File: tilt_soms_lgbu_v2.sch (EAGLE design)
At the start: 37 parts

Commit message: Added a v2 for the tilt_soms_lgbu board (tilt_soms_lgbu_v2)
Primary changes:
Placed all components on top layer including the con-wago connectors.
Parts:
- SOMS: value (none) -> JST-PH_3-PIN_HEADER; device con-wago-500:W237-103 -> SRG:JST-PH_3-PIN_HEADER
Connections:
- net FEATHER_3.3V: now also SOMS.3; no longer SOMS-1.KL
- net GND: now also SOMS.1; no longer SOMS-3.KL
- net GPIOA3: now also SOMS.2; no longer SOMS-2.KL
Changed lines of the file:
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@@
 <part name="C4" library="rcl" deviceset="C-US" device="C1812"/>
 <part name="MAIN_SWITCH" library="SRG" deviceset="JST-PH_2-PIN_HEADER" device=""/>
-<part name="SOMS" library="con-wago-500" deviceset="W237-103" device=""/>
 <part name="H5" library="holes" library_urn="urn:adsk.eagle:library:237" deviceset="MOUNT-HOLE" device="2.8" package3d_urn="urn:adsk.eagle:package:14271/1"/>
 <part name="H6" library="holes" library_urn="urn:adsk.eagle:library:237" deviceset="MOUNT-HOLE" device="2.8" package3d_urn="urn:adsk.eagle:package:14271/1"/>
 <part name="H7" library="holes" library_urn="urn:adsk.eagle:library:237" deviceset="MOUNT-HOLE" device="2.8" package3d_urn="urn:adsk.eagle:package:14271/1"/>
 <part name="H8" library="holes" library_urn="urn:adsk.eagle:library:237" deviceset="MOUNT-HOLE" device="2.8" package3d_urn="urn:adsk.eagle:package:14271/1"/>
+<part name="SOMS" library="SRG" deviceset="JST-PH_3-PIN_HEADER" device=""/>
 </parts>
 <sheets>
@@
 <instance part="C4" gate="G$1" x="320.04" y="215.9"/>
 <instance part="MAIN_SWITCH" gate="G$1" x="160.02" y="101.6" smashed="yes" rot="R90"/>
-<instance part="SOMS" gate="-1" x="287.02" y="132.08"/>
-<instance part="SOMS" gate="-2" x="287.02" y="127"/>
-<instance part="SOMS" gate="-3" x="287.02" y="121.92"/>
 <instance part="H5" gate="G$1" x="20.32" y="63.5"/>
 <instance part="H6" gate="G$1" x="20.32" y="55.88"/>
 <instance part="H7" gate="G$1" x="20.32" y="71.12"/>
 <instance part="H8" gate="G$1" x="20.32" y="78.74"/>
+<instance part="SOMS" gate="G$1" x="271.78" y="127" rot="R180"/>
 </instances>
 <busses>
@@
 </segment>
 <segment>
-<wire x1="299.72" y1="124.46" x2="309.88" y2="124.46" width="0.1524" layer="91"/>
-<pinref part="SOMS" gate="-3" pin="KL"/>
-<wire x1="299.72" y1="124.46" x2="299.72" y2="121.92" width="0.1524" layer="91"/>
-<wire x1="299.72" y1="121.92" x2="292.1" y2="121.92" width="0.1524" layer="91"/>
+<pinref part="SOMS" gate="G$1" pin="1"/>
+<wire x1="276.86" y1="124.46" x2="309.88" y2="124.46" width="0.1524" layer="91"/>
 </segment>
 <segment>
@@
 </segment>
 <segment>
-<wire x1="294.64" y1="129.54" x2="309.88" y2="129.54" width="0.1524" layer="91"/>
 <label x="299.72" y="129.54" size="1.778" layer="95"/>
-<wire x1="294.64" y1="129.54" x2="294.64" y2="132.08" width="0.1524" layer="91"/>
-<pinref part="SOMS" gate="-1" pin="KL"/>
-<wire x1="294.64" y1="132.08" x2="292.1" y2="132.08" width="0.1524" layer="91"/>
+<pinref part="SOMS" gate="G$1" pin="3"/>
+<wire x1="276.86" y1="129.54" x2="309.88" y2="129.54" width="0.1524" layer="91"/>
 </segment>
 </net>
@@
 </segment>
 <segment>
-<wire x1="292.1" y1="127" x2="320.04" y2="127" width="0.1524" layer="91"/>
+<wire x1="276.86" y1="127" x2="320.04" y2="127" width="0.1524" layer="91"/>
 <label x="322.58" y="127" size="1.778" layer="95" rot="R180"/>
-<pinref part="SOMS" gate="-2" pin="KL"/>
-</segment>
-</net>
+<pinref part="SOMS" gate="G$1" pin="2"/>
+</segment>
+</net>

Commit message: Reversed board. Snap to mills grid.
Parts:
- removed H5, H6, H7, H8: MOUNT-HOLE2.8, holes:MOUNT-HOLE2.8
- R1, R2, R3, R4: device rcl:R-EU_0204/5 -> rcl:R-EU_0204/7
- SOMS: value JST-PH_3-PIN_HEADER -> TERMINAL-BLOCK-3.5MM-3-PIN-LONG-PAD; device SRG:JST-PH_3-PIN_HEADER -> Rembrandt Electronics - Terminal Block 3-5mm v1-0:TERMINAL-BLOCK-3.5MM-3-PIN-LONG-PAD
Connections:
- net FEATHER_3.3V: now also SOMS-3.K; no longer SOMS.3
- net GND: now also SOMS-1.K; no longer SOMS.1
- net GPIOA3: now also SOMS-2.K; no longer SOMS.2
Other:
- moved on the sheet: U$3

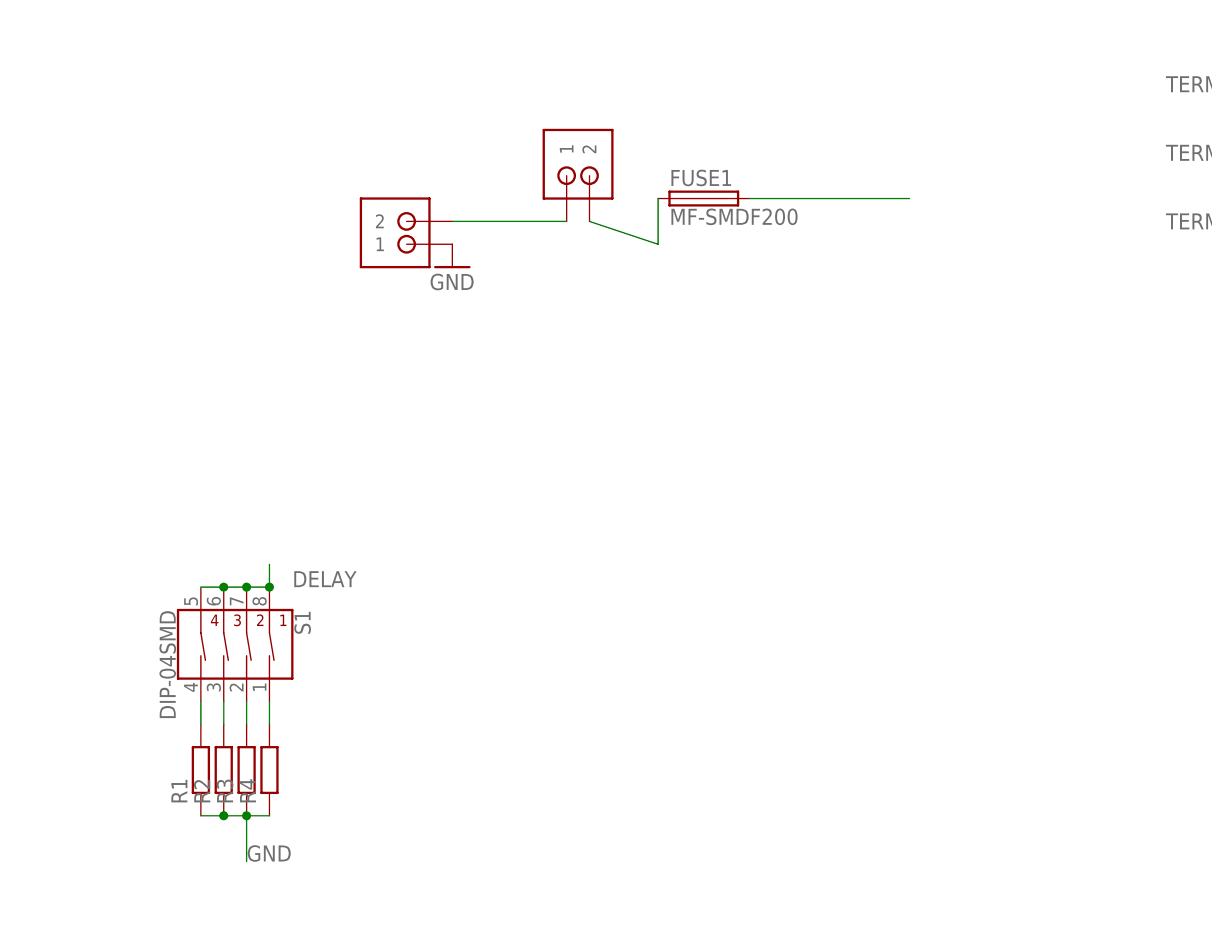
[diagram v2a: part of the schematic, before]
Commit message: no dip switch
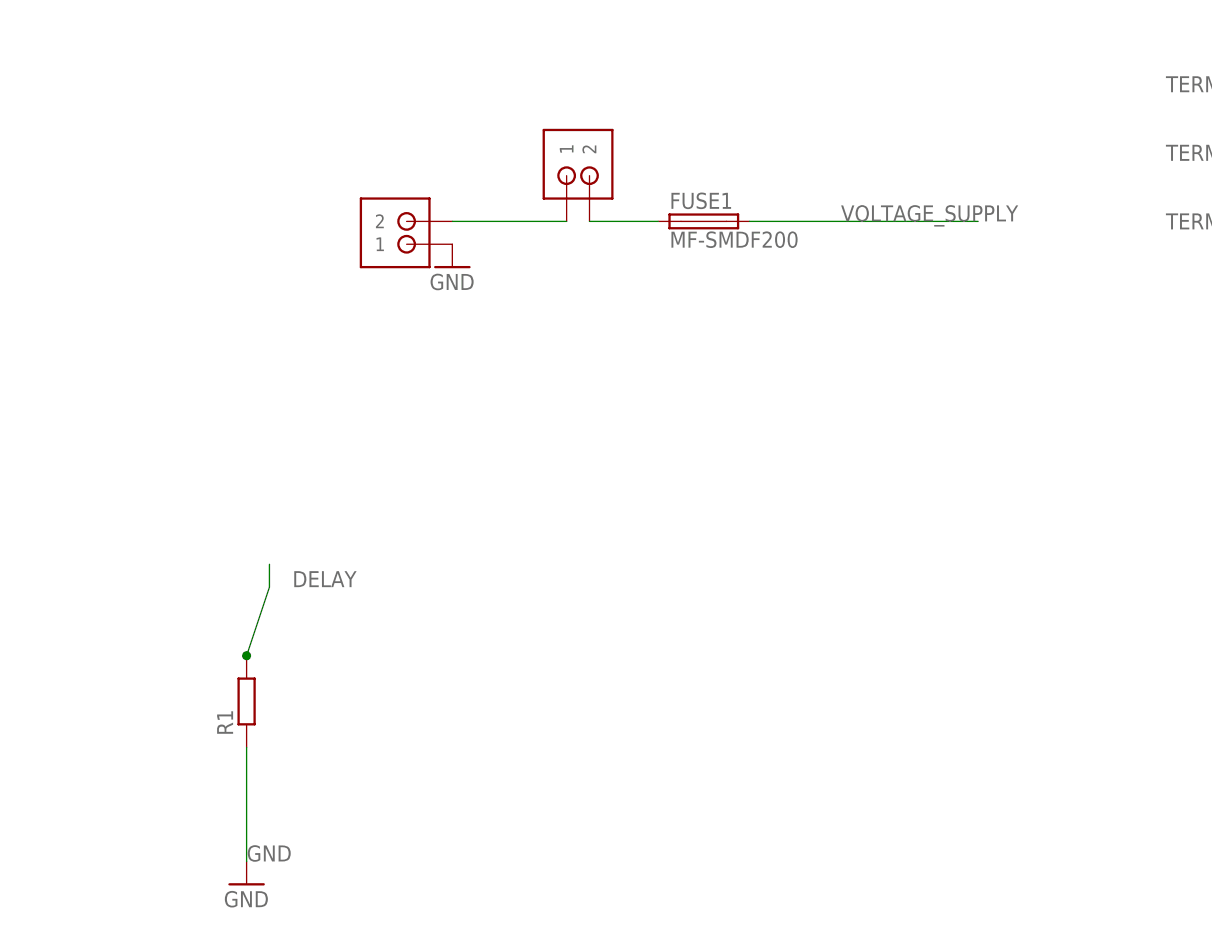
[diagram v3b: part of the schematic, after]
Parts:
- removed R2, R3, R4: (no value), rcl:R-EU_0204/7
- removed S1: DIP-04SMD, SparkFun-Switches:DIP-04SMD
- R1: device rcl:R-EU_0204/7 -> rcl:R-EU_0309/12
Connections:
- removed net N$10: R2.2, S1.3A
- removed net N$11: R3.2, S1.2A
- removed net N$12: R4.2, S1.1A
- removed net N$9: R1.2, S1.4A
- net DELAY: now also R1.2; no longer S1.1B, S1.2B, S1.3B, S1.4B
- net GND: no longer R2.1, R3.1, R4.1
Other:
- moved on the sheet: FUSE1, R1
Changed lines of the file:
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@@
 <part name="BATT" library="SRG" deviceset="JST-PH_2-PIN_HEADER" device=""/>
 <part name="U$3" library="edc_modules" deviceset="TPL5110_BREAKOUT" device=""/>
-<part name="S1" library="SparkFun-Switches" deviceset="DIP-04" device="SMD"/>
-<part name="R1" library="rcl" deviceset="R-EU_" device="0204/7"/>
-<part name="R2" library="rcl" deviceset="R-EU_" device="0204/7"/>
-<part name="R3" library="rcl" deviceset="R-EU_" device="0204/7"/>
-<part name="R4" library="rcl" deviceset="R-EU_" device="0204/7"/>
+<part name="R1" library="rcl" deviceset="R-EU_" device="0309/12"/>
 <part name="FRAME2" library="frames" deviceset="DINA4_L" device=""/>
 <part name="U$4" library="edc_modules" deviceset="BNO05_BREAKOUT" device=""/>
@@
 <part name="MAIN_SWITCH" library="SRG" deviceset="JST-PH_2-PIN_HEADER" device=""/>
 <part name="SOMS" library="Rembrandt Electronics - Terminal Block 3-5mm v1-0" deviceset="TERMINAL-BLOCK-3.5MM-3-PIN" device="-LONG-PAD"/>
+<part name="GND1" library="supply1" deviceset="GND" device=""/>
 </parts>
 <sheets>
@@
 <instance part="BATT" gate="G$1" x="137.16" y="93.98" smashed="yes" rot="R180"/>
 <instance part="U$3" gate="G$1" x="96.52" y="137.16"/>
-<instance part="S1" gate="G$1" x="127" y="50.8" rot="R180"/>
-<instance part="R1" gate="G$1" x="116.84" y="33.02" rot="R90"/>
-<instance part="R2" gate="G$1" x="119.38" y="33.02" rot="R90"/>
-<instance part="R3" gate="G$1" x="121.92" y="33.02" rot="R90"/>
-<instance part="R4" gate="G$1" x="124.46" y="33.02" rot="R90"/>
+<instance part="R1" gate="G$1" x="121.92" y="40.64" rot="R90"/>
 <instance part="FRAME2" gate="G$2" x="325.12" y="0"/>
 <instance part="U$4" gate="G$1" x="281.94" y="149.86"/>
@@
 <attribute name="NAME" x="318.643" y="158.1658" size="1.778" layer="95" rot="R180"/>
 </instance>
-<instance part="FUSE1" gate="A" x="172.72" y="96.52"/>
+<instance part="FUSE1" gate="A" x="172.72" y="93.98"/>
 <instance part="C3" gate="G$1" x="309.88" y="215.9"/>
 <instance part="C4" gate="G$1" x="320.04" y="215.9"/>
@@
 <instance part="SOMS" gate="-2" x="284.48" y="101.6" rot="R180"/>
 <instance part="SOMS" gate="-3" x="284.48" y="109.22" rot="R180"/>
+<instance part="GND1" gate="1" x="121.92" y="20.32"/>
 </instances>
 <busses>
@@
 <segment>
 <pinref part="R1" gate="G$1" pin="1"/>
-<pinref part="R2" gate="G$1" pin="1"/>
-<wire x1="116.84" y1="27.94" x2="119.38" y2="27.94" width="0.1524" layer="91"/>
-<pinref part="R3" gate="G$1" pin="1"/>
-<wire x1="119.38" y1="27.94" x2="121.92" y2="27.94" width="0.1524" layer="91"/>
-<junction x="119.38" y="27.94"/>
-<pinref part="R4" gate="G$1" pin="1"/>
-<wire x1="121.92" y1="27.94" x2="124.46" y2="27.94" width="0.1524" layer="91"/>
-<junction x="121.92" y="27.94"/>
-<wire x1="121.92" y1="27.94" x2="121.92" y2="22.86" width="0.1524" layer="91"/>
+<wire x1="121.92" y1="35.56" x2="121.92" y2="22.86" width="0.1524" layer="91"/>
 <label x="121.92" y="22.86" size="1.778" layer="95"/>
+<pinref part="GND1" gate="1" pin="GND"/>
 </segment>
 <segment>
@@
 <segment>
 <pinref part="FUSE1" gate="A" pin="2"/>
-<wire x1="177.8" y1="96.52" x2="195.58" y2="96.52" width="0.1524" layer="91"/>
+<wire x1="177.8" y1="93.98" x2="203.2" y2="93.98" width="0.1524" layer="91"/>
+<label x="187.96" y="93.98" size="1.778" layer="95"/>
 </segment>
 </net>
@@
 </segment>
 <segment>
-<pinref part="S1" gate="G$1" pin="4B"/>
-<pinref part="S1" gate="G$1" pin="3B"/>
-<wire x1="116.84" y1="53.34" x2="119.38" y2="53.34" width="0.1524" layer="91"/>
-<pinref part="S1" gate="G$1" pin="2B"/>
-<wire x1="119.38" y1="53.34" x2="121.92" y2="53.34" width="0.1524" layer="91"/>
-<junction x="119.38" y="53.34"/>
-<pinref part="S1" gate="G$1" pin="1B"/>
-<wire x1="121.92" y1="53.34" x2="124.46" y2="53.34" width="0.1524" layer="91"/>
-<junction x="121.92" y="53.34"/>
+<wire x1="121.92" y1="45.72" x2="124.46" y2="53.34" width="0.1524" layer="91"/>
 <wire x1="124.46" y1="53.34" x2="124.46" y2="55.88" width="0.1524" layer="91"/>
-<junction x="124.46" y="53.34"/>
 <label x="127" y="53.34" size="1.778" layer="95"/>
-</segment>
-</net>
-<net name="N$9" class="0">
-<segment>
-<pinref part="S1" gate="G$1" pin="4A"/>
 <pinref part="R1" gate="G$1" pin="2"/>
-<wire x1="116.84" y1="40.64" x2="116.84" y2="38.1" width="0.1524" layer="91"/>
-</segment>
-</net>
-<net name="N$10" class="0">
-<segment>
-<pinref part="S1" gate="G$1" pin="3A"/>
-<pinref part="R2" gate="G$1" pin="2"/>
-<wire x1="119.38" y1="40.64" x2="119.38" y2="38.1" width="0.1524" layer="91"/>
-</segment>
-</net>
-<net name="N$11" class="0">
-<segment>
-<pinref part="S1" gate="G$1" pin="2A"/>
-<pinref part="R3" gate="G$1" pin="2"/>
-<wire x1="121.92" y1="40.64" x2="121.92" y2="38.1" width="0.1524" layer="91"/>
-</segment>
-</net>
-<net name="N$12" class="0">
-<segment>
-<pinref part="S1" gate="G$1" pin="1A"/>
-<pinref part="R4" gate="G$1" pin="2"/>
-<wire x1="124.46" y1="40.64" x2="124.46" y2="38.1" width="0.1524" layer="91"/>
+<junction x="121.92" y="45.72"/>
 </segment>
 </net>
@@
 <segment>
 <pinref part="MAIN_SWITCH" gate="G$1" pin="2"/>
-<wire x1="160.02" y1="93.98" x2="167.64" y2="91.44" width="0.1524" layer="91"/>
+<wire x1="160.02" y1="93.98" x2="167.64" y2="93.98" width="0.1524" layer="91"/>
 <pinref part="FUSE1" gate="A" pin="1"/>
-<wire x1="167.64" y1="91.44" x2="167.64" y2="96.52" width="0.1524" layer="91"/>
-</segment>
-</net>
+</segment>
+</net>
